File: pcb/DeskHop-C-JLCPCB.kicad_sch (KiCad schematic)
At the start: 6 parts, among them U101 Digital Isolator

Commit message: Update schematic with MPN/LCSC, and update manual BOM.
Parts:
- C101, C102: value 100nf -> 100n; LCSC C2858367 -> C541405; MPN (none) -> CC0402KRX5R5BB104
- U101: MPN (none) -> ISO7721DR
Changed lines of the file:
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@@
+      (effects (font (size 1.27 1.27)) hide)
+    )
+    (property "MPN" "ISO7721DR" (at 142.24 90.17 0)
       (effects (font (size 1.27 1.27)) hide)
     )
@@
       (effects (font (size 1.27 1.27)) (justify left))
     )
-    (property "Value" "100nf" (at 111.76 77.47 0)
+    (property "Value" "100n" (at 111.76 77.47 0)
       (effects (font (size 1.27 1.27)) (justify left))
     )
@@
       (effects (font (size 1.27 1.27)) hide)
     )
-    (property "LCSC" "C2858367" (at 107.95 76.2 0)
+    (property "LCSC" "C541405" (at 107.95 76.2 0)
+      (effects (font (size 1.27 1.27)) hide)
+    )
+    (property "MPN" "CC0402KRX5R5BB104" (at 107.95 76.2 0)
       (effects (font (size 1.27 1.27)) hide)
     )
@@
       (effects (font (size 1.27 1.27)) (justify left))
     )
-    (property "Value" "100nf" (at 180.34 77.47 0)
+    (property "Value" "100n" (at 180.34 77.47 0)
       (effects (font (size 1.27 1.27)) (justify left))
     )
@@
       (effects (font (size 1.27 1.27)) hide)
     )
-    (property "LCSC" "C2858367" (at 176.53 76.2 0)
+    (property "LCSC" "C541405" (at 176.53 76.2 0)
       (effects (font (size 1.27 1.27)) hide)
     )
+    (property "MPN" "CC0402KRX5R5BB104" (at 176.53 76.2 0)
+      (effects (font (size 1.27 1.27)) hide)
+    )

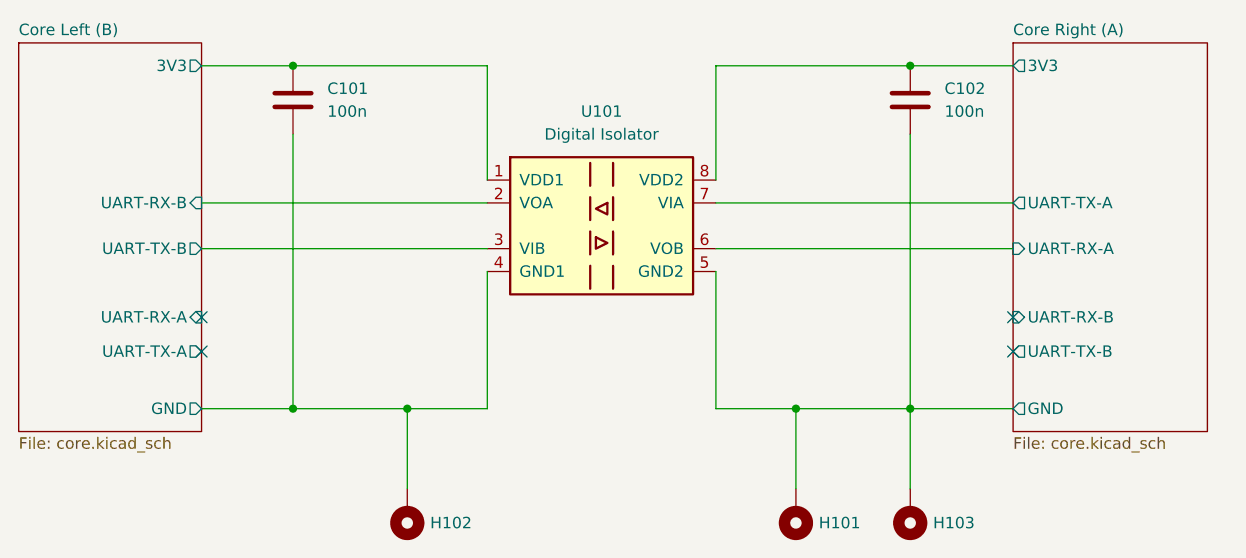
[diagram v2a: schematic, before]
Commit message: Use better net labels for UART links.
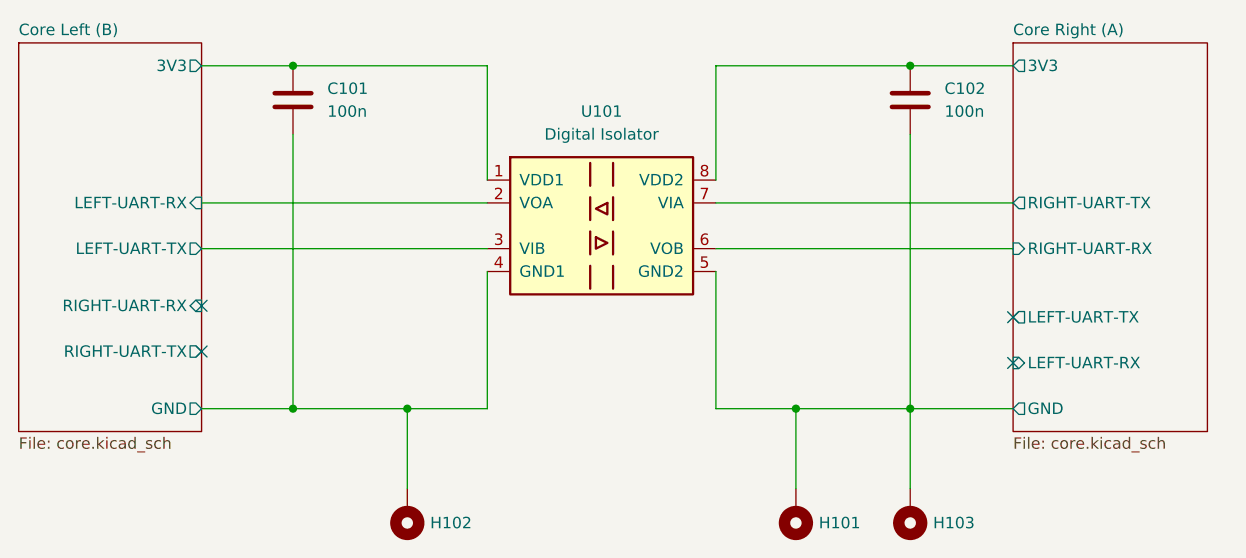
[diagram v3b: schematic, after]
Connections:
- net Core Left (B)/UART-RX-B renamed Core Left (B)/LEFT-UART-RX
- net Core Left (B)/UART-TX-B renamed Core Left (B)/LEFT-UART-TX
- net Core Right (A)/UART-RX-A renamed Core Right (A)/RIGHT-UART-RX
- net Core Right (A)/UART-TX-A renamed Core Right (A)/RIGHT-UART-TX
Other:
- sheet Core Left (B) ports: added LEFT-UART-RX, LEFT-UART-TX, RIGHT-UART-RX, RIGHT-UART-TX; removed UART-RX-A, UART-RX-B, UART-TX-A, UART-TX-B
- sheet Core Right (A) ports: added LEFT-UART-RX, LEFT-UART-TX, RIGHT-UART-RX, RIGHT-UART-TX; removed UART-RX-A, UART-RX-B, UART-TX-A, UART-TX-B
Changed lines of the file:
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@@
   )
   (no_connect (at 187.96 100.33))
-  (no_connect (at 97.79 100.33))
+  (no_connect (at 97.79 99.06))
   (no_connect (at 97.79 104.14))
-  (no_connect (at 187.96 104.14))
+  (no_connect (at 187.96 105.41))
   (wire (pts (xy 163.83 110.49) (xy 163.83 119.38))
     (stroke (width 0) (type default))
@@
       (effects (font (size 1.27 1.27)) (justify left))
     )
-    (pin "UART-TX-B" output (at 187.96 104.14 180)
-      (effects (font (size 1.27 1.27)) (justify left))
-    )
-    (pin "UART-RX-B" input (at 187.96 100.33 180)
-      (effects (font (size 1.27 1.27)) (justify left))
-    )
-    (pin "UART-TX-A" output (at 187.96 87.63 180)
-      (effects (font (size 1.27 1.27)) (justify left))
-    )
-    (pin "UART-RX-A" input (at 187.96 92.71 180)
+    (pin "LEFT-UART-TX" output (at 187.96 100.33 180)
+      (effects (font (size 1.27 1.27)) (justify left))
+    )
+    (pin "LEFT-UART-RX" input (at 187.96 105.41 180)
+      (effects (font (size 1.27 1.27)) (justify left))
+    )
+    (pin "RIGHT-UART-TX" output (at 187.96 87.63 180)
+      (effects (font (size 1.27 1.27)) (justify left))
+    )
+    (pin "RIGHT-UART-RX" input (at 187.96 92.71 180)
       (effects (font (size 1.27 1.27)) (justify left))
     )
@@
       (effects (font (size 1.27 1.27)) (justify right))
     )
-    (pin "UART-TX-B" output (at 97.79 92.71 0)
-      (effects (font (size 1.27 1.27)) (justify right))
-    )
-    (pin "UART-RX-B" input (at 97.79 87.63 0)
-      (effects (font (size 1.27 1.27)) (justify right))
-    )
-    (pin "UART-TX-A" output (at 97.79 104.14 0)
-      (effects (font (size 1.27 1.27)) (justify right))
-    )
-    (pin "UART-RX-A" input (at 97.79 100.33 0)
-      (effects (font (size 1.27 1.27)) (justify right))
-    )
+    (pin "LEFT-UART-TX" output (at 97.79 92.71 0)
+      (effects (font (size 1.27 1.27)) (justify right))
+    )
+    (pin "LEFT-UART-RX" input (at 97.79 87.63 0)
+      (effects (font (size 1.27 1.27)) (justify right))
+    )
+    (pin "RIGHT-UART-TX" output (at 97.79 104.14 0)
+      (effects (font (size 1.27 1.27)) (justify right))
+    )
+    (pin "RIGHT-UART-RX" input (at 97.79 99.06 0)
+      (effects (font (size 1.27 1.27)) (justify right))
+    )
